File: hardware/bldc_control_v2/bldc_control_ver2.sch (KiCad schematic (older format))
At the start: 63 parts, among them IC1 6N136, IC2 6N136, IC3 6N136, IC4 6N136, IC5 6N136, P1 CONN_01X04, P2 CONN_01X03, P3 CONN_01X06, P4 CONN_01X08, P5 CONN_01X04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

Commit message: first: remove old versions of the hardware - git history rulez. second: made schematic a bit more readable... third: migrated schematic to KiCAD 4
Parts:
- C1, C10, C12, C13, C14, C16, C17, C2, C3, C6, C7, C8, C9: symbol C -> C-RESCUE-bldc_control_ver2
- C15: value C -> C15; footprint Capacitors_SMD:C_1206 -> (none)
- C4, C5: value C -> 18p; symbol C -> C-RESCUE-bldc_control_ver2
- D1, D2, D3: symbol LED -> LED-RESCUE-bldc_control_ver2
- IC1, IC2, IC3, IC4, IC5: symbol 6N136 -> 6N136-RESCUE-bldc_control_ver2
- R1, R13, R14, R15, R2, R20, R21, R22, R23, R24, R25, R3, R4, R5, R6, R7: symbol R -> R-RESCUE-bldc_control_ver2
- R10, R11, R12, R8, R9: footprint Resistors_SMD:R_0805 -> (none)
- R16: value R -> 10k; symbol R -> R-RESCUE-bldc_control_ver2
- R17, R18, R19: value R -> 220; symbol R -> R-RESCUE-bldc_control_ver2
- U1: symbol NCP1117ST33T3G -> NCP1117ST33T3G-RESCUE-bldc_control_ver2
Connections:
- wire segments 194 -> 114
- no-connect marks 0 -> 20
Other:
- note added: "3.3 volts power supply for stm32"
- note added: "Debug UART"
- note added: "ENABLE, STEP, DIR:\ninputs - opto-isolated"
- note added: "Opto-Isolated Inputs for magnetic encoder"
- note added: "SWD program plug"
- note added: "dual voltage bus transceiver\nand voltage level converter"
- note added: "hall resolver"
- note added: "integrated magnetic resolver"
- note added: "optocoupler up to 10MHz"
- note added: "power supply selection jumper\n3.3V or 5.0V"
- moved on the sheet: C1, C10, C11, C12, C13, C14, C16, C17, C2, C3, C4, C5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

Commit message: tempfiles vom KiCAD entfernt und Bauteilwerte ausgedacht...
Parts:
- C1, C12, C13, C14, C17, C2, C3, C6, C7: value C -> 100n; footprint Capacitors_SMD:C_1206 -> Capacitors_SMD:C_0603
- C10, C8, C9: value C -> 10µ; footprint Capacitors_SMD:C_1206 -> Capacitors_SMD:C_0805
- C15: value C15 -> 100n; footprint (none) -> Capacitors_SMD:C_0603
- C16: value C -> 100n
- C4, C5: footprint Capacitors_SMD:C_1206 -> Capacitors_SMD:C_0603
- D1, D2, D3: footprint LEDs:LED-0805 -> LEDs:LED_0603
- R1, R2, R3, R4, R5: value R -> 220; footprint Resistors_SMD:R_0805 -> Resistors_SMD:R_0603
- R10, R11, R12, R8, R9: value R -> 10k; footprint (none) -> Resistors_SMD:R_0603
- R13, R6, R7: value R -> 10k; footprint Resistors_SMD:R_0805 -> Resistors_SMD:R_0603
- R14, R15, R16, R17, R18, R19, R20, R21, R22, R23, R24, R25: footprint Resistors_SMD:R_0805 -> Resistors_SMD:R_0603
- U1: footprint acronet:SOT223_S -> TO_SOT_Packages_SMD:SOT-223-3Lead_TabPin2
- X1: value CRYSTAL -> 8MHz
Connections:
- no-connect marks 20 -> 21
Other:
- note added: "Opto-Isolated Inputs for magnetic encoder\nmaximum input voltage: 5VDC"
- note added: "optocoupler up to 2MHz\nmaximum input voltage: 5VDC"
- note removed: "Opto-Isolated Inputs for magnetic encoder"
- note removed: "optocoupler up to 10MHz"
- moved on the sheet: IC4, IC5, R11, R12, R14, R15, R20, R21, R22, R23, R24, R25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

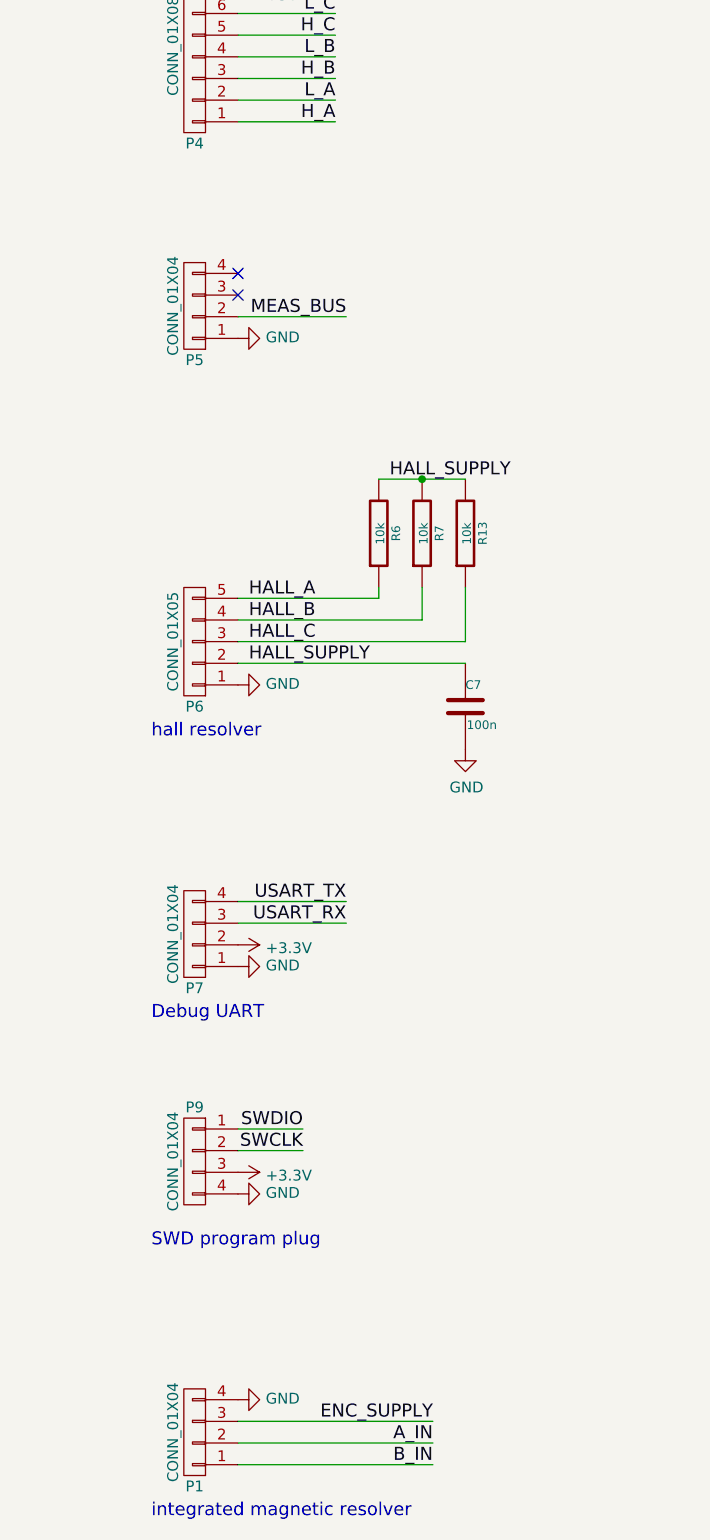
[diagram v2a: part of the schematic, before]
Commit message: schaltplan und layout angepasst
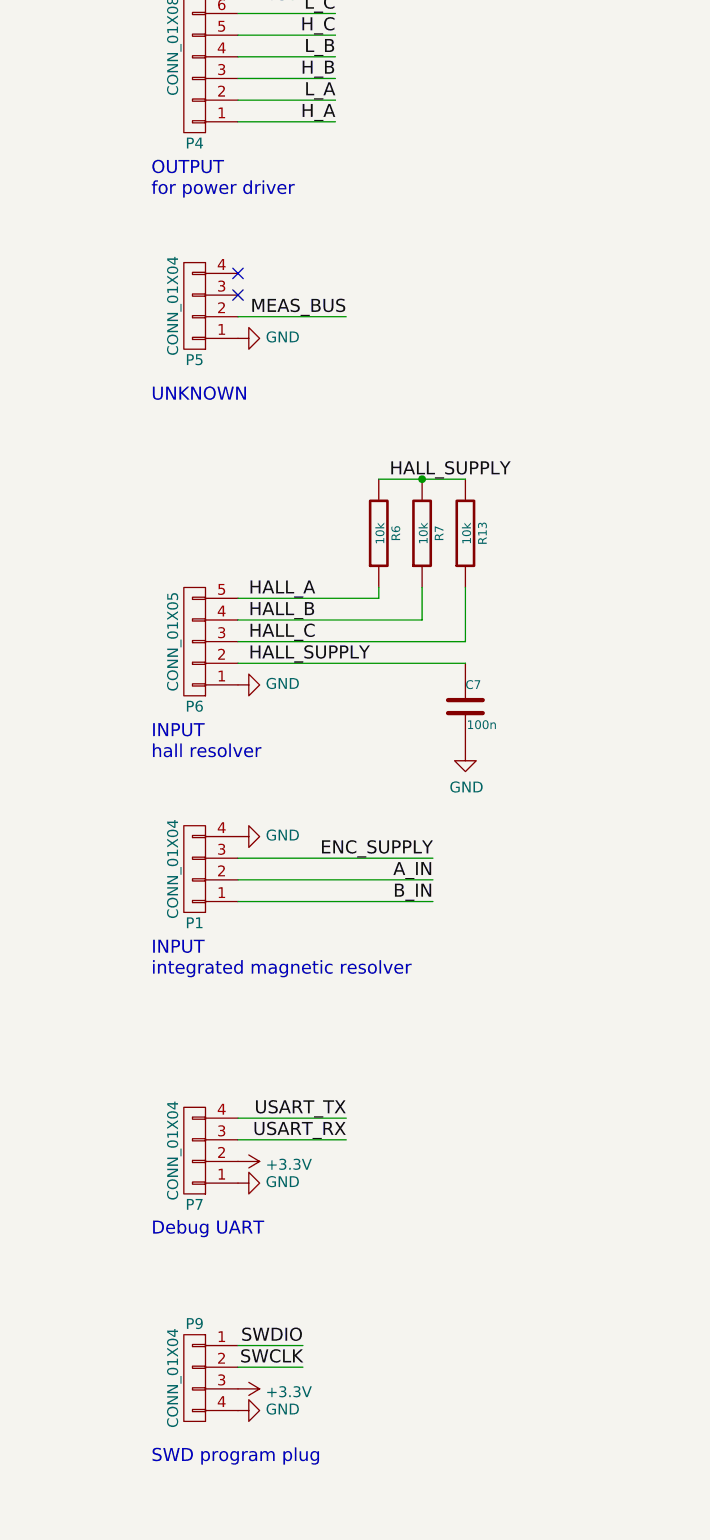
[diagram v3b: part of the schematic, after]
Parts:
- P1: footprint w_conn_screw:mors_4p -> Connectors_JST:JST_PH_B4B-PH-K_04x2.00mm_Straight
- P4: footprint Pin_Headers:Pin_Header_Straight_1x08 -> Connectors_JST:JST_PH_B8B-PH-K_08x2.00mm_Straight
- P6: footprint w_conn_screw:mors_5p -> Connectors_JST:JST_XH_B05B-XH-A_05x2.50mm_Straight
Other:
- note added: "INPUT\nhall resolver"
- note added: "INPUT\nintegrated magnetic resolver"
- note added: "OUTPUT\nfor power driver"
- note added: "UNKNOWN"
- note removed: "hall resolver"
- note removed: "integrated magnetic resolver"
- moved on the sheet: P1, P7, P9
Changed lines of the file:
@@
 F 0 "P4" H 2100 3750 50  0000 C CNN
 F 1 "CONN_01X08" V 2200 3300 50  0000 C CNN
-F 2 "Pin_Headers:Pin_Header_Straight_1x08" H 2100 3300 60  0001 C CNN
+F 2 "Connectors_JST:JST_PH_B8B-PH-K_08x2.00mm_Straight" H 2100 3300 60  0001 C CNN
 F 3 "" H 2100 3300 60  0000 C CNN
 	1    2100 3300
@@
 F 0 "P6" H 2100 6350 50  0000 C CNN
 F 1 "CONN_01X05" V 2200 6050 50  0000 C CNN
-F 2 "w_conn_screw:mors_5p" H 2100 6050 60  0001 C CNN
+F 2 "Connectors_JST:JST_XH_B05B-XH-A_05x2.50mm_Straight" H 2100 6050 60  0001 C CNN
 F 3 "" H 2100 6050 60  0000 C CNN
 	1    2100 6050
@@
 L CONN_01X04 P9
 U 1 1 562B0392
-P 2100 8450
-F 0 "P9" H 2100 8700 50  0000 C CNN
-F 1 "CONN_01X04" V 2200 8450 50  0000 C CNN
-F 2 "jst-ph:jst-ph-JST-PH4" H 2100 8450 60  0001 C CNN
-F 3 "" H 2100 8450 60  0000 C CNN
-	1    2100 8450
+P 2100 9450
+F 0 "P9" H 2100 9700 50  0000 C CNN
+F 1 "CONN_01X04" V 2200 9450 50  0000 C CNN
+F 2 "jst-ph:jst-ph-JST-PH4" H 2100 9450 60  0001 C CNN
+F 3 "" H 2100 9450 60  0000 C CNN
+	1    2100 9450
 	-1   0    0    -1
 $EndComp
 Wire Wire Line
-	2300 8300 2600 8300
-Wire Wire Line
-	2600 8400 2300 8400
-Text Label 2600 8300 2    60   ~ 0
+	2300 9300 2600 9300
+Wire Wire Line
+	2600 9400 2300 9400
+Text Label 2600 9300 2    60   ~ 0
 SWDIO
-Text Label 2600 8400 2    60   ~ 0
+Text Label 2600 9400 2    60   ~ 0
 SWCLK
 $Comp
 L CONN_01X04 P7
 U 1 1 562B1330
-P 2100 7400
-F 0 "P7" H 2100 7650 50  0000 C CNN
-F 1 "CONN_01X04" V 2200 7400 50  0000 C CNN
-F 2 "Pin_Headers:Pin_Header_Straight_1x04" H 2100 7400 60  0001 C CNN
-F 3 "" H 2100 7400 60  0000 C CNN
-	1    2100 7400
+P 2100 8400
+F 0 "P7" H 2100 8650 50  0000 C CNN
+F 1 "CONN_01X04" V 2200 8400 50  0000 C CNN
+F 2 "Pin_Headers:Pin_Header_Straight_1x04" H 2100 8400 60  0001 C CNN
+F 3 "" H 2100 8400 60  0000 C CNN
+	1    2100 8400
 	-1   0    0    1
 $EndComp
 Wire Wire Line
-	2300 7250 2800 7250
-Wire Wire Line
-	2300 7350 2800 7350
-Text Label 2800 7250 2    60   ~ 0
+	2300 8250 2800 8250
+Wire Wire Line
+	2300 8350 2800 8350
+Text Label 2800 8250 2    60   ~ 0
 USART_TX
-Text Label 2800 7350 2    60   ~ 0
+Text Label 2800 8350 2    60   ~ 0
 USART_RX
 Wire Wire Line
@@
 L CONN_01X04 P1
 U 1 1 562C8FFA
-P 2100 9700
-F 0 "P1" H 2100 9950 50  0000 C CNN
-F 1 "CONN_01X04" V 2200 9700 50  0000 C CNN
-F 2 "w_conn_screw:mors_4p" H 2100 9700 60  0001 C CNN
-F 3 "" H 2100 9700 60  0000 C CNN
-	1    2100 9700
+P 2100 7100
+F 0 "P1" H 2100 7350 50  0000 C CNN
+F 1 "CONN_01X04" V 2200 7100 50  0000 C CNN
+F 2 "Connectors_JST:JST_PH_B4B-PH-K_04x2.00mm_Straight" H 2100 7100 60  0001 C CNN
+F 3 "" H 2100 7100 60  0000 C CNN
+	1    2100 7100
 	-1   0    0    1
 $EndComp
 Wire Wire Line
-	2300 9750 3200 9750
-Wire Wire Line
-	2300 9850 3200 9850
+	2300 7150 3200 7150
+Wire Wire Line
+	2300 7250 3200 7250
 $Comp
 L CONN_01X06 P3
@@
 Wire Wire Line
 	1850 1450 1850 1400
-Text Label 3200 9650 2    60   ~ 0
+Text Label 3200 7050 2    60   ~ 0
 ENC_SUPPLY
 Wire Wire Line
-	2300 9650 3200 9650
-Text Label 3200 9750 2    60   ~ 0
+	2300 7050 3200 7050
+Text Label 3200 7150 2    60   ~ 0
 A_IN
-Text Label 3200 9850 2    60   ~ 0
+Text Label 3200 7250 2    60   ~ 0
 B_IN
 $Comp
@@
 L GND #PWR030
 U 1 1 58AB8226
-P 2300 7550
-F 0 "#PWR030" H 2300 7300 50  0001 C CNN
-F 1 "GND" V 2305 7422 50  0000 R CNN
-F 2 "" H 2300 7550 50  0000 C CNN
-F 3 "" H 2300 7550 50  0000 C CNN
-	1    2300 7550
+P 2300 8550
+F 0 "#PWR030" H 2300 8300 50  0001 C CNN
+F 1 "GND" V 2305 8422 50  0000 R CNN
+F 2 "" H 2300 8550 50  0000 C CNN
+F 3 "" H 2300 8550 50  0000 C CNN
+	1    2300 8550
 	0    -1   -1   0
 $EndComp
@@
 L +3.3V #PWR031
 U 1 1 58AB83AE
-P 2300 7450
-F 0 "#PWR031" H 2300 7300 50  0001 C CNN
-F 1 "+3.3V" V 2315 7578 50  0000 L CNN
-F 2 "" H 2300 7450 50  0000 C CNN
-F 3 "" H 2300 7450 50  0000 C CNN
-	1    2300 7450
+P 2300 8450
+F 0 "#PWR031" H 2300 8300 50  0001 C CNN
+F 1 "+3.3V" V 2315 8578 50  0000 L CNN
+F 2 "" H 2300 8450 50  0000 C CNN
+F 3 "" H 2300 8450 50  0000 C CNN
+	1    2300 8450
 	0    1    1    0
 $EndComp
@@
 L +3.3V #PWR032
 U 1 1 58AB9DD4
-P 2300 8500
-F 0 "#PWR032" H 2300 8350 50  0001 C CNN
-F 1 "+3.3V" V 2315 8628 50  0000 L CNN
-F 2 "" H 2300 8500 50  0000 C CNN
-F 3 "" H 2300 8500 50  0000 C CNN
-	1    2300 8500
+P 2300 9500
+F 0 "#PWR032" H 2300 9350 50  0001 C CNN
+F 1 "+3.3V" V 2315 9628 50  0000 L CNN
+F 2 "" H 2300 9500 50  0000 C CNN
+F 3 "" H 2300 9500 50  0000 C CNN
+	1    2300 9500
 	0    1    1    0
 $EndComp
@@
 L GND #PWR033
 U 1 1 58AB9EA5
-P 2300 8600
-F 0 "#PWR033" H 2300 8350 50  0001 C CNN
-F 1 "GND" V 2305 8472 50  0000 R CNN
-F 2 "" H 2300 8600 50  0000 C CNN
-F 3 "" H 2300 8600 50  0000 C CNN
-	1    2300 8600
+P 2300 9600
+F 0 "#PWR033" H 2300 9350 50  0001 C CNN
+F 1 "GND" V 2305 9472 50  0000 R CNN
+F 2 "" H 2300 9600 50  0000 C CNN
+F 3 "" H 2300 9600 50  0000 C CNN
+	1    2300 9600
 	0    -1   -1   0
 $EndComp
-Text Notes 1900 8850 0    60   ~ 0
+Text Notes 1900 9850 0    60   ~ 0
 SWD program plug
-Text Notes 1900 7800 0    60   ~ 0
+Text Notes 1900 8800 0    60   ~ 0
 Debug UART
-Text Notes 1900 6500 0    60   ~ 0
-hall resolver
+Text Notes 1900 6600 0    60   ~ 0
+INPUT\nhall resolver
 Text Notes 12500 6200 0    60   ~ 0
 dual voltage bus transceiver\nand voltage level converter
@@
 L GND #PWR062
 U 1 1 58ACE797
-P 2300 9550
-F 0 "#PWR062" H 2300 9300 50  0001 C CNN
-F 1 "GND" V 2305 9422 50  0000 R CNN
-F 2 "" H 2300 9550 50  0000 C CNN
-F 3 "" H 2300 9550 50  0000 C CNN
-	1    2300 9550
+P 2300 6950
+F 0 "#PWR062" H 2300 6700 50  0001 C CNN
+F 1 "GND" V 2305 6822 50  0000 R CNN
+F 2 "" H 2300 6950 50  0000 C CNN
+F 3 "" H 2300 6950 50  0000 C CNN
+	1    2300 6950
 	0    -1   -1   0
 $EndComp
@@
 Text Notes 6500 9700 0    60   ~ 0
 optocoupler up to 2MHz\nmaximum input voltage: 5VDC
-Text Notes 1900 10100 0    60   ~ 0
-integrated magnetic resolver
+Text Notes 1900 7600 0    60   ~ 0
+INPUT\nintegrated magnetic resolver
 $Comp
 L +5V #PWR075
@@
 NoConn ~ 9700 4950
 NoConn ~ 10650 9250
+Text Notes 1900 4000 0    60   ~ 0
+OUTPUT\nfor power driver
+Text Notes 1900 4950 0    60   ~ 0
+UNKNOWN
 $EndSCHEMATC
